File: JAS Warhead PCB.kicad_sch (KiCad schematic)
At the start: 27 parts, among them J1 Conn_01x02_Socket, J10 Conn_01x02_Socket, J11 Conn_01x02_Socket, J12 Conn_01x02_Pin, J13 Conn_01x02_Pin, J14 Conn_01x02_Pin, J2 Conn_01x02_Socket, J7 Conn_01x02_Socket, K3 Panasonic_ALFG1PF12, K4 Panasonic_ALFG1PF12, Q1 PN2222A, Q2 PN2222A, U4 LD1117S50TR_SOT223

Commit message: refresh stage 1
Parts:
- added D11: 1N4001, Diode_THT:D_DO-41_SOD81_P10.16mm_Horizontal, symbol Diode:1N4001
- added J15: Conn_01x02_Socket, TerminalBlock:TerminalBlock_bornier-2_P5.08mm, symbol Connector:Conn_01x02_Socket
- added J16, J17: Conn_01x03_Pin, Connector_PinHeader_2.54mm:PinHeader_1x03_P2.54mm_Vertical, symbol Connector:Conn_01x03_Pin
- added K1: Panasonic_ALFG1PF12, Relay_THT:Relay_SPST_Panasonic_ALFG_FormA_CircularHoles, symbol Relay:Panasonic_ALFG1PF12
- added Q3: PN2222A, Package_TO_SOT_THT:TO-92_Inline, symbol Transistor_BJT:PN2222A
- added R13: 4.7K, Resistor_SMD:R_0815_2038Metric, symbol Device:R
- added R16: 50K, Resistor_THT:R_Axial_DIN0207_L6.3mm_D2.5mm_P10.16mm_Horizontal, symbol Device:R
- added R17, R19: 5K, Resistor_THT:R_Axial_DIN0207_L6.3mm_D2.5mm_P10.16mm_Horizontal, symbol Device:R
- added R18, R20: 2K, Resistor_THT:R_Axial_DIN0207_L6.3mm_D2.5mm_P10.16mm_Horizontal, symbol Device:R
- added R23, R24: 1K, symbol Device:R
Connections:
- net +12V: now also K1.14, Q3.3 (C)
- net +5V: now also J16.1 (Pin_1), J17.1 (Pin_1)
- net 3V3: now also R23.2, R24.1
- net GND: now also J15.1 (Pin_1), J16.3 (Pin_3), J17.3 (Pin_3), R16.2, R18.2, R20.2
- net SCL: now also R24.2
- net SDA: now also R23.1
- new net: J17.2 (Pin_2), R19.1
- new net: D11.2 (A), Q3.1 (E)
- new net: Q3.2 (B), R13.1
- new net: J15.2 (Pin_2), K1.11
- new net: D11.1 (K), K1.A1
- new net: K1.A2, R16.1
- new net: J16.2 (Pin_2), R17.1
- new net OIL_Press: R17.2, R18.1
- new net RELAY3: R13.2
- new net WTR_Press: R19.2, R20.1
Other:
- added sheet Load Cell (LOADCELL.kicad_sch)
- note added: "Oil Pressure with logic level converter"
- note added: "Spark Plug Relay"
- note added: "TODO Remove nonsensical Diodes on SPI Lanes Re-vamp the connections for relays Connect load cell properly Re-work board placement entirely Generate BOM to work with JLC manufacturing Re-think the LDO and potentially add more power to the board Completely re-consider the size of certain things on the board, most capacitors and resistors can be 0603, except load bearing / buring resistors"
- note added: "Water Pressure with logic level converter"
- moved on the sheet: D1, D10, J1, J12, J13, J14, J2, J7, K3, K4, Q1, Q2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

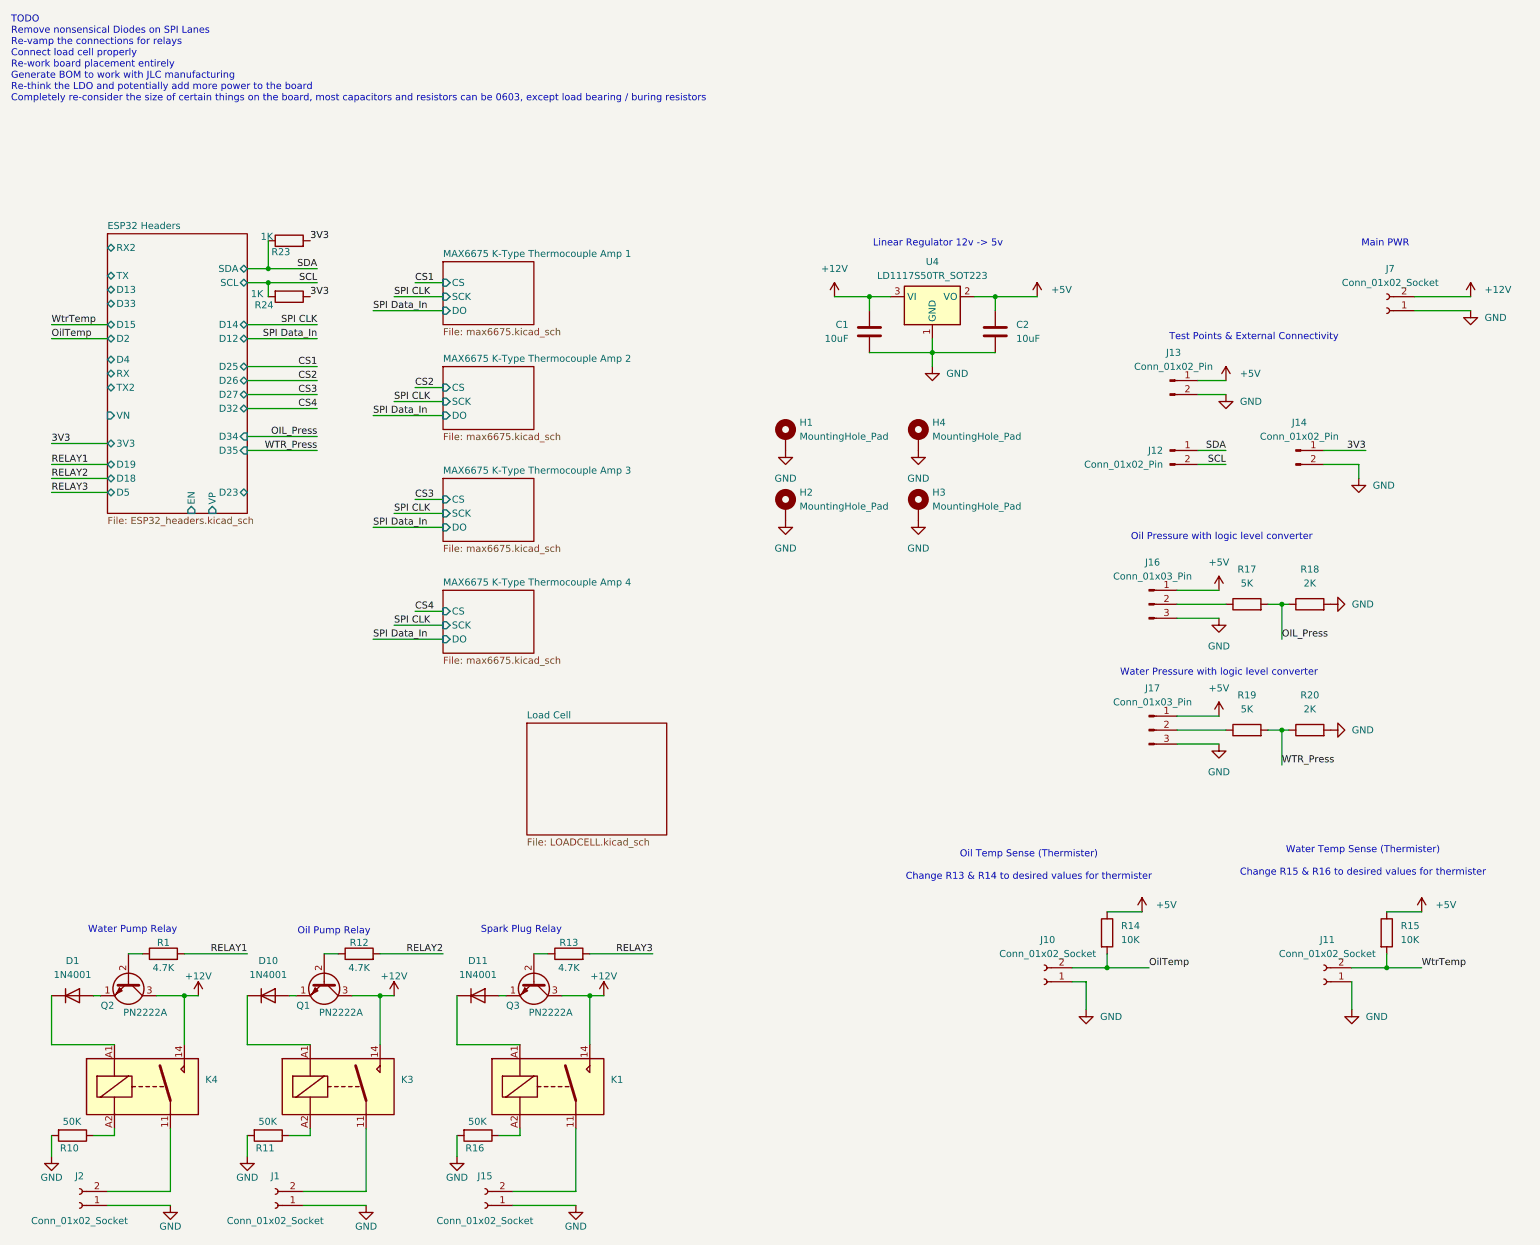
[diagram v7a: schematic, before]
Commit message: progress toward final board, need smaller relays
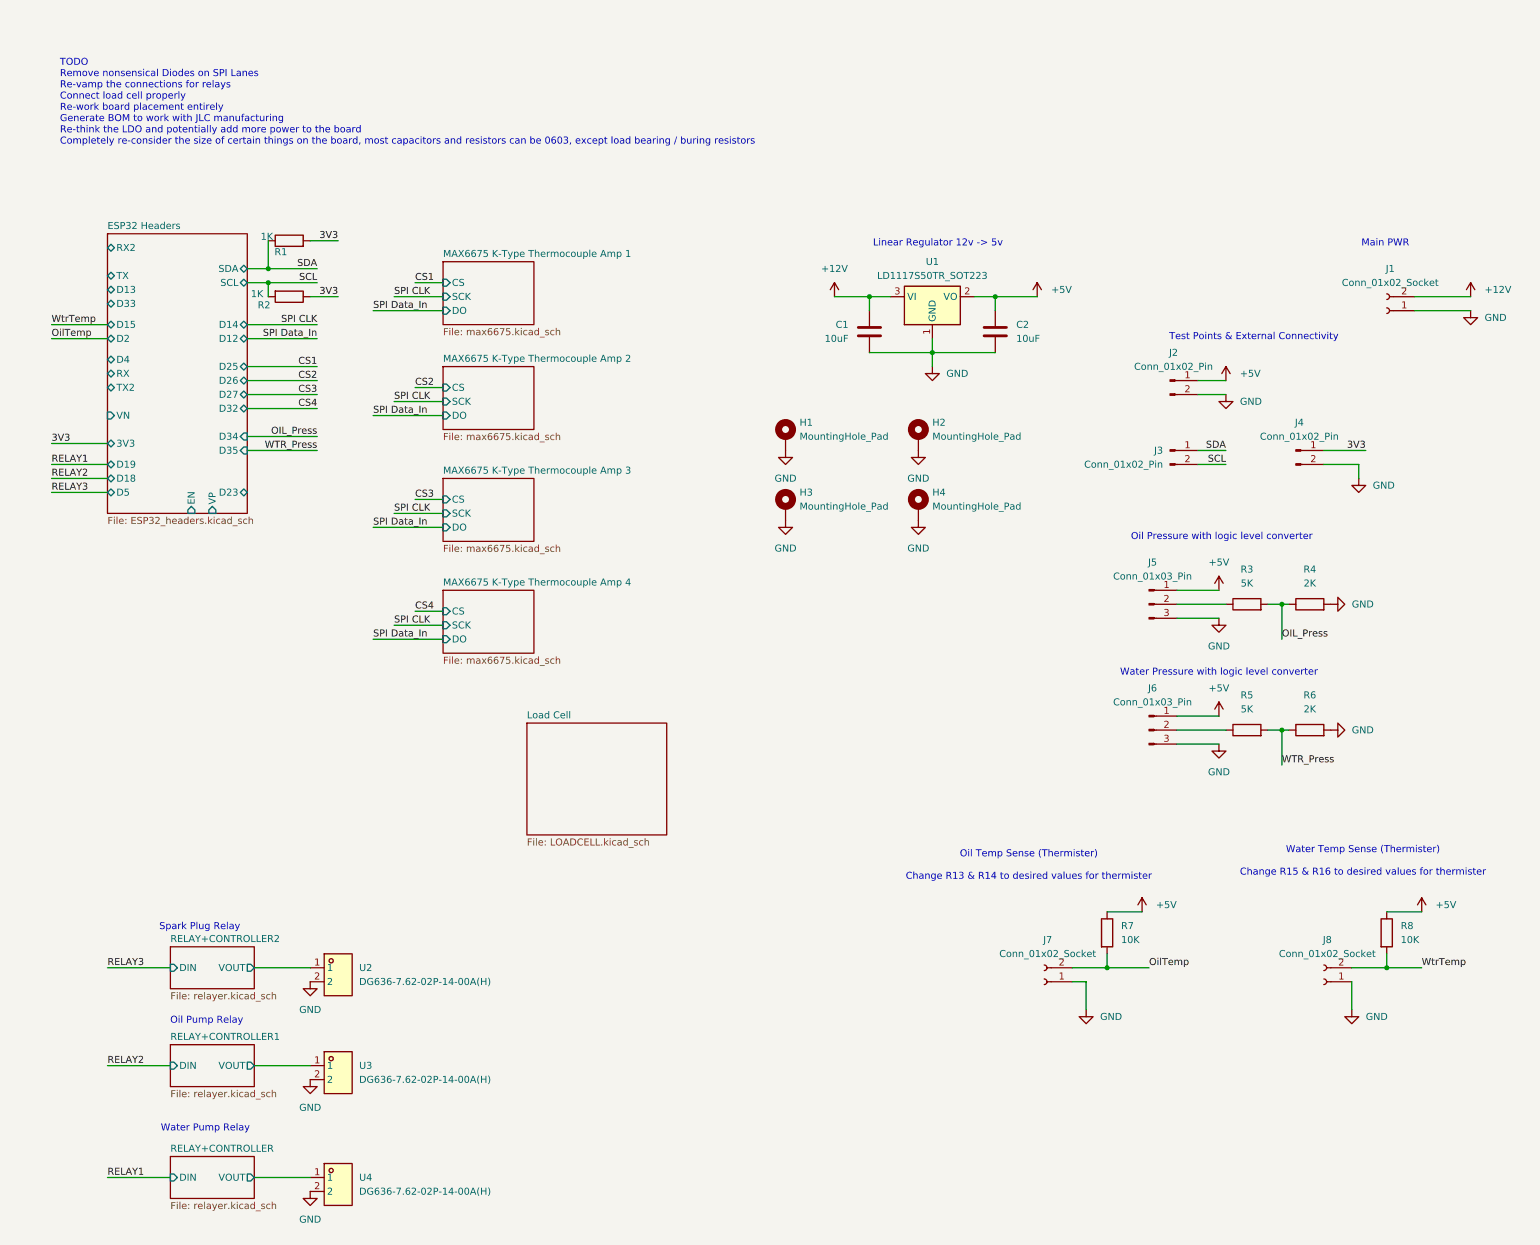
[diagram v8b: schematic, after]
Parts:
- removed D1, D10, D11: 1N4001, Diode_THT:D_DO-41_SOD81_P10.16mm_Horizontal, symbol Diode:1N4001
- removed J1, J15, J2: Conn_01x02_Socket, TerminalBlock:TerminalBlock_bornier-2_P5.08mm, symbol Connector:Conn_01x02_Socket
- removed K1, K3, K4: Panasonic_ALFG1PF12, Relay_THT:Relay_SPST_Panasonic_ALFG_FormA_CircularHoles, symbol Relay:Panasonic_ALFG1PF12
- removed Q1, Q2, Q3: PN2222A, Package_TO_SOT_THT:TO-92_Inline, symbol Transistor_BJT:PN2222A
- removed R1, R12, R13: 4.7K, Resistor_SMD:R_0815_2038Metric, symbol Device:R
- removed R10, R11, R16: 50K, Resistor_THT:R_Axial_DIN0207_L6.3mm_D2.5mm_P10.16mm_Horizontal, symbol Device:R
- added U2, U3, U4: DG636-7.62-02P-14-00A(H), dg636:CONN-TH_DG636-7.62-02P-14-0, symbol dg636:DG636-7.62-02P-14-00A(H)
- C1: footprint Capacitor_SMD:C_0805_2012Metric -> Capacitor_SMD:C_0402_1005Metric
- R1: renamed from R23; footprint (none) -> Resistor_SMD:R_0603_1608Metric
- R2: renamed from R24; footprint (none) -> Resistor_SMD:R_0603_1608Metric
- R3: renamed from R17; footprint Resistor_THT:R_Axial_DIN0207_L6.3mm_D2.5mm_P10.16mm_Horizontal -> Resistor_SMD:R_0603_1608Metric
- R4: renamed from R18; footprint Resistor_THT:R_Axial_DIN0207_L6.3mm_D2.5mm_P10.16mm_Horizontal -> Resistor_SMD:R_0603_1608Metric
- R5: renamed from R19; footprint Resistor_THT:R_Axial_DIN0207_L6.3mm_D2.5mm_P10.16mm_Horizontal -> Resistor_SMD:R_0603_1608Metric
- R6: renamed from R20; footprint Resistor_THT:R_Axial_DIN0207_L6.3mm_D2.5mm_P10.16mm_Horizontal -> Resistor_SMD:R_0603_1608Metric
- R7: renamed from R14; footprint Resistor_THT:R_Axial_DIN0207_L6.3mm_D2.5mm_P10.16mm_Horizontal -> Resistor_SMD:R_0603_1608Metric
- R8: renamed from R15; footprint Resistor_THT:R_Axial_DIN0207_L6.3mm_D2.5mm_P10.16mm_Horizontal -> Resistor_SMD:R_0603_1608Metric
- renumbered H4 to H2, H2 to H3, H3 to H4, J7 to J1, J13 to J2, J12 to J3, J14 to J4, J16 to J5, J17 to J6, J10 to J7, J11 to J8, U4 to U1
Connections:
- net GND: now also U2.2, U3.2, U4.2
- new net RELAY+CONTROLLER/VOUT: U4.1
- new net RELAY+CONTROLLER1/VOUT: U3.1
- new net RELAY+CONTROLLER2/VOUT: U2.1
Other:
- added sheet RELAY+CONTROLLER (relayer.kicad_sch)
- added sheet RELAY+CONTROLLER1 (relayer.kicad_sch)
- added sheet RELAY+CONTROLLER2 (relayer.kicad_sch)
